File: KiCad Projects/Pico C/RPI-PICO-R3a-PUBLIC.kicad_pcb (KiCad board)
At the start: 2 copper layers, 53.7 x 21 mm, 54 parts, among them J3 USB_C_Receptacle_USB2.0_16P, J4 SM03B-SRSS-TB, Q1 DMG1012T-7, SW1 PTS810 SJM 250 SMTR LFSPTS810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, U1 RP2040, U2 RT6150B-33GQW, U3 W25Q16JVUXIQ, Y1 ECS-120-8-33-JGN-TR

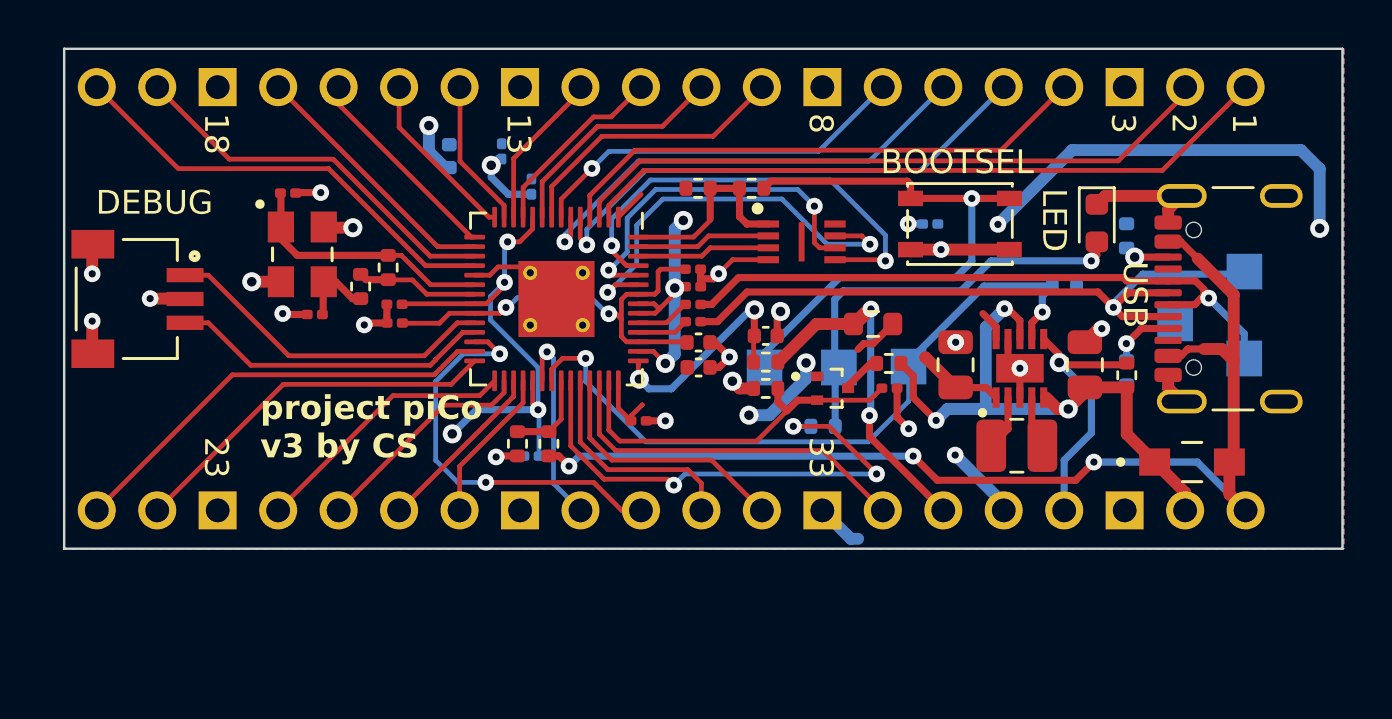
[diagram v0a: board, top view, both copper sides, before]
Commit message: Added Pico 2
Added an initial design for the Pico 2. Also updated the original Pico C to v4 (without README update since I'm waiting on boards to ship).
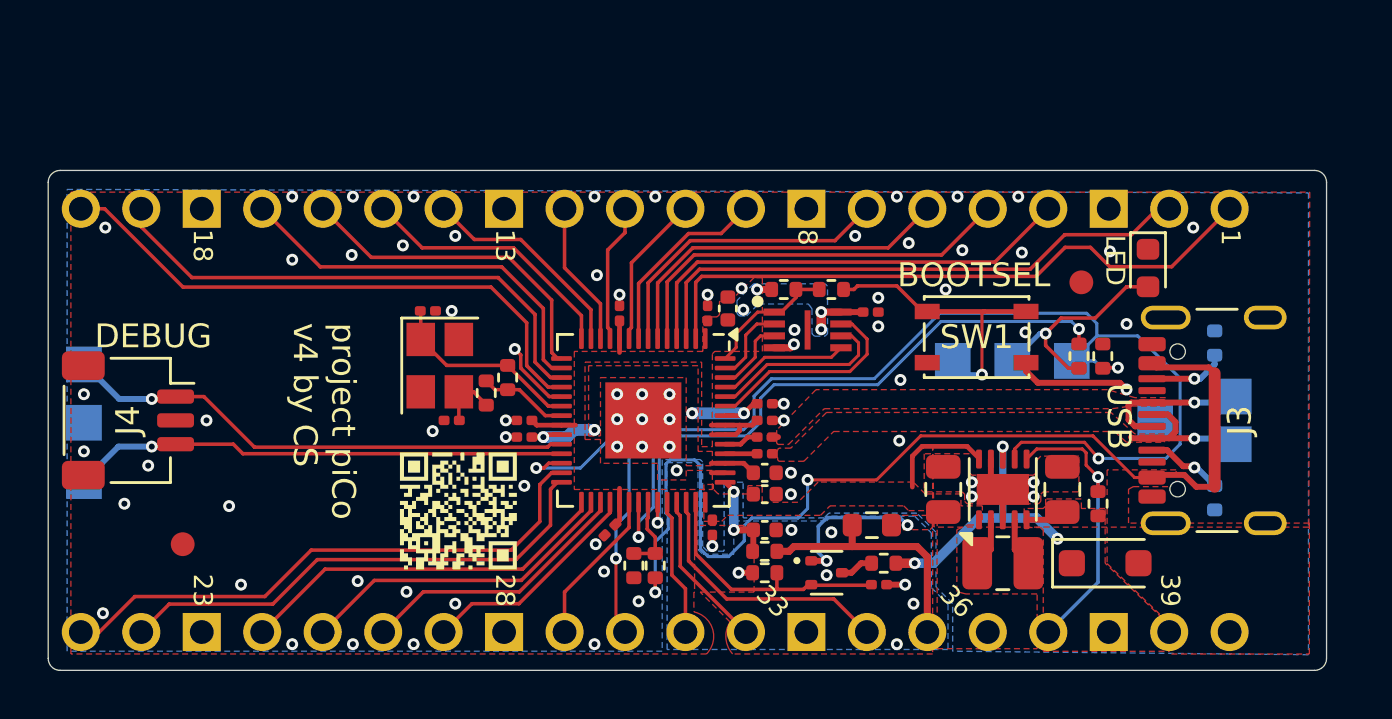
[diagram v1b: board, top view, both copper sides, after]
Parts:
- added FID1: Fiducial, Fiducial:Fiducial_1mm_Mask2mm, F.Cu at (168.3, 98.7)
- added FID2: Fiducial, Fiducial:Fiducial_1mm_Mask2mm, F.Cu at (130.6, 109.7)
- added TP7: TestPoint, TestPoint:TestPoint_Pad_1.5x1.5mm, B.Cu at (126.5, 102.2)
- added TP8: TestPoint, TestPoint:TestPoint_Pad_1.5x1.5mm, B.Cu at (126.5, 104.6)
- added TP9: TestPoint, TestPoint:TestPoint_Pad_1.5x1.5mm, B.Cu at (126.5, 107.0)
- C10, C11, C16, C17, C3, C7, C8, C9: footprint Pico_C:C_0201_0603Metric -> Capacitor_SMD:C_0201_0603Metric
- C15, C4, C5, C6: footprint Pico_C:C_0201_0603Metric -> Capacitor_SMD:C_0201_0603Metric; moved to F.Cu
- C18, R3, R8: moved to F.Cu
- D1: footprint Pico_C:DIOM3616X98N -> Diode_SMD:D_SOD-123F
- J4: footprint Pico_C:JST_SM03B-SRSS-TB_LF__SN_ -> Connector_JST:JST_SH_SM03B-SRSS-TB_1x03-1MP_P1.00mm_Horizontal
- Q1: footprint Pico_C:SOT50P160X90-3N -> Package_TO_SOT_SMD:SOT-523
- R12, R13: footprint Pico_C:R_0201_0603Metric -> Resistor_SMD:R_0201_0603Metric
- SW1: value PTS810 SJM 250 SMTR LFSPTS810 SJM 250 SMTR LFS -> PTS810 SJK 250 SMTR LFS; footprint Pico_C:SW_SPST_PTS810 -> Button_Switch_SMD:SW_SPST_PTS810
- U1: footprint Pico_C:QFN-56-1EP_7x7mm_P0.4mm_EP3.2x3.2mm_ThermalVias -> Package_DFN_QFN:QFN-56-1EP_7x7mm_P0.4mm_EP3.2x3.2mm
- U2: footprint Pico_C:SON50P250X250X80-11N -> Package_DFN_QFN:DFN-10-1EP_2.6x2.6mm_P0.5mm_EP1.3x2.2mm
- Y1: footprint Pico_C:XTAL_ECS-120-8-33-JGN-TR -> Crystal:Crystal_SMD_SeikoEpson_FA238-4Pin_3.2x2.5mm
- moved J2 14.0 mm to (150.4, 113.4)
- moved C18 13.3 mm to (153.5, 99.8)
- moved R3 11.1 mm to (168.2, 101.8), turned to -90 degrees
- moved C4 11.0 mm to (152.7, 100.0)
- moved R7 8.45 mm to (159.6, 108.9)
- moved R5 8.39 mm to (160.1, 110.5)
- moved C3 8.26 mm to (159.8, 111.4)
- moved C13 8.15 mm to (155.1, 109.1)
- moved R9 7.95 mm to (155.1, 110.0)
- moved TP6 7.91 mm to (162.9, 102.0)
- moved Q1 7.75 mm to (157.7, 110.9)
- moved R6 7.74 mm to (155.1, 110.9)
- moved C16 7.68 mm to (140.9, 99.9)
- moved Y1 7.43 mm to (141.4, 102.2)
- moved C8 7.32 mm to (144.9, 104.5)
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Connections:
- R11 pad 2: Net-(R11-Pad2) -> Net-(SW1-A)
- SW1 pad 1: Net-(R11-Pad2) -> Net-(SW1-A)
- SW1 pad 2: Net-(R11-Pad2) -> GND
- TP6 pad 1: Net-(R11-Pad2) -> Net-(SW1-A)
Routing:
- net +3V3: track 75.3 -> 22.8 mm, vias 15 -> 6
- net GND: track 42.8 -> 14.4 mm, vias 19 -> 83
- net Net-(R11-Pad2): track 24.6 -> 0.00 mm, vias 1 -> 0
- net USB_DM: track 29.4 -> 6.36 mm
- net USB_DP: track 27.3 -> 6.52 mm
- net GPIO23: track 30.6 -> 47.2 mm, vias 2 -> 3
- net QSPI_SD0: track 19.1 -> 5.55 mm, vias 2 -> 0
- net Net-(SW1-A): track 0.00 -> 12.3 mm, vias 0 -> 1
- net VS: track 25.2 -> 13.1 mm
- net +1V1: track 18.2 -> 9.22 mm, vias 2 -> 4
- net QSPI_SD3: track 17.4 -> 8.87 mm, vias 2 -> 0
- net Net-(D2-A): track 17.8 -> 9.30 mm
- net SWCLK: track 14.1 -> 21.6 mm, vias 0 -> 1
- net SWDIO: track 13.5 -> 20.9 mm, vias 0 -> 1
- net QSPI_SCLK: track 15.0 -> 7.70 mm, vias 2 -> 0
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- added copper zone on F.Cu, net +1V1
- added copper zone on B.Cu, net +3V3
- added copper zone on F.Cu, net GND
- added copper zone on F.Cu, net USB_DM
- added copper zone on F.Cu, net USB_DP
- added copper zone on F.Cu, net VBUS
- added copper zone on F.Cu, net VS
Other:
- outline, holes or cut-outs redrawn
- board text added: "CLK"
- board text added: "DIO"
- board text added: "GND"
- board text added: "project piCo v4 by CS"
- board text removed: "project piCo v3 by CS"
